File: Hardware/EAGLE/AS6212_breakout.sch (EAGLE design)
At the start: 19 parts, among them J2 QWIIC_RIGHT_ANGLE, J3 QWIIC_RIGHT_ANGLE, U1 AS6212

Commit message: v01 main push
Updated Eagle files and source software
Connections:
- net ADD1: now also J1.1; no longer J1.2
- net GND: now also J1.2; no longer J1.1
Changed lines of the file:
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@@
 <part name="P+2" library="supply1" library_urn="urn:adsk.eagle:library:371" deviceset="VCC" device=""/>
 <part name="P+3" library="supply1" library_urn="urn:adsk.eagle:library:371" deviceset="VCC" device=""/>
-<part name="GND3" library="supply1" library_urn="urn:adsk.eagle:library:371" deviceset="GND" device=""/>
 <part name="P+4" library="supply1" library_urn="urn:adsk.eagle:library:371" deviceset="VCC" device=""/>
 <part name="P+5" library="supply1" library_urn="urn:adsk.eagle:library:371" deviceset="VCC" device=""/>
@@
 <part name="R3" library="SparkFun-Resistors" deviceset="330OHM" device="-0603-1/10W-1%" value="330"/>
 <part name="JP7" library="SparkFun-Jumpers" deviceset="JUMPER-SMT_2_NC_TRACE" device="_SILK" package3d_urn="urn:adsk.eagle:package:39281/1"/>
+<part name="GND3" library="supply1" library_urn="urn:adsk.eagle:library:371" deviceset="GND" device=""/>
 </parts>
 <sheets>
@@
 <attribute name="VALUE" x="142.24" y="162.56" size="1.778" layer="96" rot="R180"/>
 </instance>
-<instance part="GND3" gate="1" x="139.7" y="139.7" smashed="yes">
-<attribute name="VALUE" x="137.16" y="137.16" size="1.778" layer="96"/>
-</instance>
 <instance part="P+4" gate="VCC" x="180.34" y="160.02" smashed="yes">
 <attribute name="VALUE" x="182.88" y="162.56" size="1.778" layer="96" rot="R180"/>
@@
 </instance>
 <instance part="JP7" gate="G$1" x="45.72" y="78.74" smashed="yes" rot="R90"/>
+<instance part="GND3" gate="1" x="147.32" y="139.7" smashed="yes">
+<attribute name="VALUE" x="144.78" y="137.16" size="1.778" layer="96"/>
+</instance>
 </instances>
 <busses>
@@
 </segment>
 <segment>
-<pinref part="J1" gate="G$1" pin="1"/>
-<wire x1="137.16" y1="144.78" x2="139.7" y2="144.78" width="0.1524" layer="91"/>
-<wire x1="139.7" y1="144.78" x2="139.7" y2="142.24" width="0.1524" layer="91"/>
-<pinref part="GND3" gate="1" pin="GND"/>
-</segment>
-<segment>
 <pinref part="J2" gate="G$1" pin="1"/>
 <wire x1="170.18" y1="144.78" x2="175.26" y2="144.78" width="0.1524" layer="91"/>
@@
 <wire x1="45.72" y1="63.5" x2="45.72" y2="60.96" width="0.1524" layer="91"/>
 </segment>
+<segment>
+<pinref part="J1" gate="G$1" pin="2"/>
+<pinref part="GND3" gate="1" pin="GND"/>
+<wire x1="137.16" y1="147.32" x2="147.32" y2="147.32" width="0.1524" layer="91"/>
+<wire x1="147.32" y1="147.32" x2="147.32" y2="142.24" width="0.1524" layer="91"/>
+</segment>
 </net>
 <net name="ADD1" class="0">
@@
 </segment>
 <segment>
-<pinref part="J1" gate="G$1" pin="2"/>
-<wire x1="137.16" y1="147.32" x2="139.7" y2="147.32" width="0.1524" layer="91"/>
-<label x="139.7" y="147.32" size="1.27" layer="95" xref="yes"/>
-</segment>
-<segment>
 <pinref part="JP6" gate="G$1" pin="2"/>
 <wire x1="195.58" y1="55.88" x2="198.12" y2="55.88" width="0.1524" layer="91"/>
 <label x="198.12" y="55.88" size="1.27" layer="95" xref="yes"/>
 </segment>
-</net>
+<segment>
+<pinref part="J1" gate="G$1" pin="1"/>
+<wire x1="137.16" y1="144.78" x2="139.7" y2="144.78" width="0.1524" layer="91"/>
+<label x="139.7" y="144.78" size="1.27" layer="95" xref="yes"/>
+</segment>
+</net>

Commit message: Rev 02 push
First production version of breakout board - push ready
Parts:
- R3: value 330 -> 10k; device SparkFun-Resistors:330OHM-0603-1/10W-1% -> SparkFun-Resistors:10KOHM-0603-1/10W-1%
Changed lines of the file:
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@@
 <part name="GND6" library="supply1" library_urn="urn:adsk.eagle:library:371" deviceset="GND" device=""/>
 <part name="P+7" library="supply1" library_urn="urn:adsk.eagle:library:371" deviceset="VCC" device=""/>
-<part name="R3" library="SparkFun-Resistors" deviceset="330OHM" device="-0603-1/10W-1%" value="330"/>
+<part name="R3" library="SparkFun-Resistors" deviceset="10KOHM" device="-0603-1/10W-1%" value="10k"/>
 <part name="JP7" library="SparkFun-Jumpers" deviceset="JUMPER-SMT_2_NC_TRACE" device="_SILK" package3d_urn="urn:adsk.eagle:package:39281/1"/>
 <part name="GND3" library="supply1" library_urn="urn:adsk.eagle:library:371" deviceset="GND" device=""/>

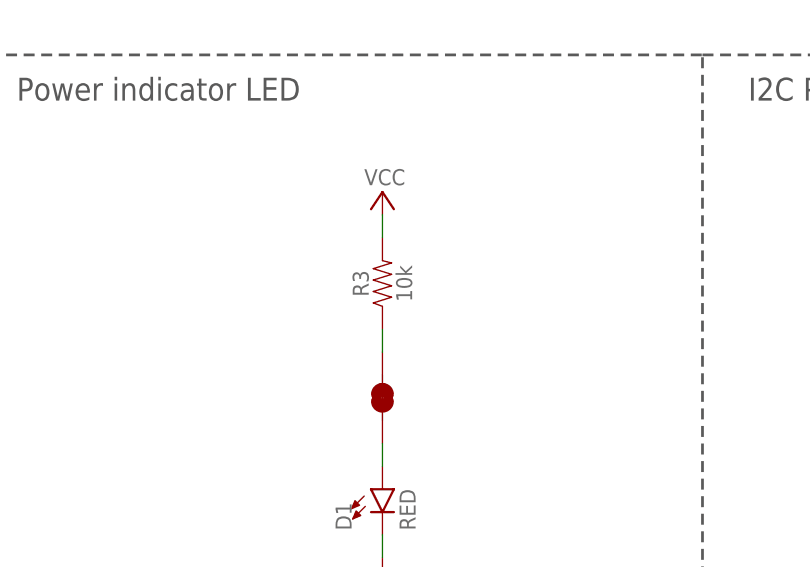
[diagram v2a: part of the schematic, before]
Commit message: Configuration register updates
small changes to software and hardware.
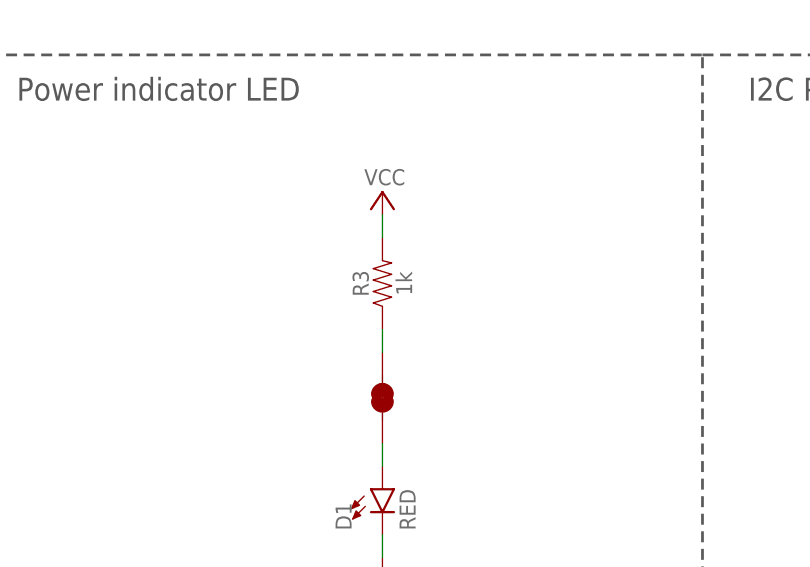
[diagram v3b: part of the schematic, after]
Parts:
- R3: value 10k -> 1k; device SparkFun-Resistors:10KOHM-0603-1/10W-1% -> SparkFun-Resistors:1KOHM-0603-1/10W-1%
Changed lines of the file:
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@@
 <part name="GND6" library="supply1" library_urn="urn:adsk.eagle:library:371" deviceset="GND" device=""/>
 <part name="P+7" library="supply1" library_urn="urn:adsk.eagle:library:371" deviceset="VCC" device=""/>
-<part name="R3" library="SparkFun-Resistors" deviceset="10KOHM" device="-0603-1/10W-1%" value="10k"/>
+<part name="R3" library="SparkFun-Resistors" deviceset="1KOHM" device="-0603-1/10W-1%" value="1k"/>
 <part name="JP7" library="SparkFun-Jumpers" deviceset="JUMPER-SMT_2_NC_TRACE" device="_SILK" package3d_urn="urn:adsk.eagle:package:39281/1"/>
 <part name="GND3" library="supply1" library_urn="urn:adsk.eagle:library:371" deviceset="GND" device=""/>

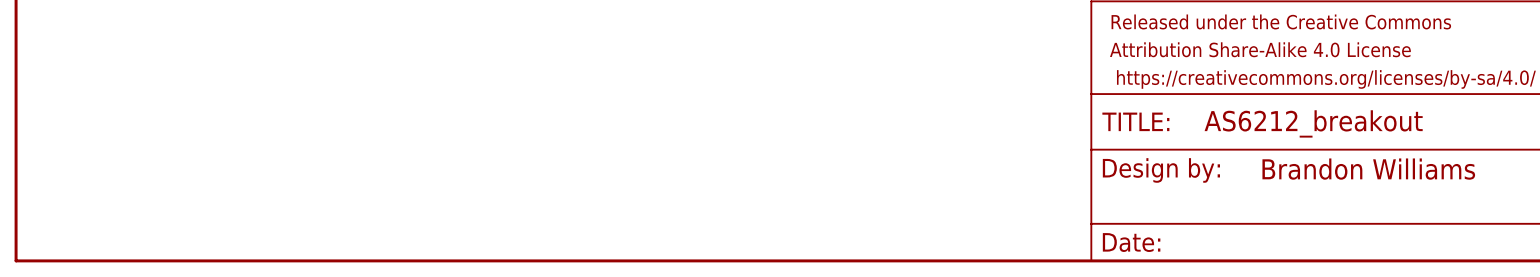
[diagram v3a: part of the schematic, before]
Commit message: Bug fixes
Added thank you in schematic as well
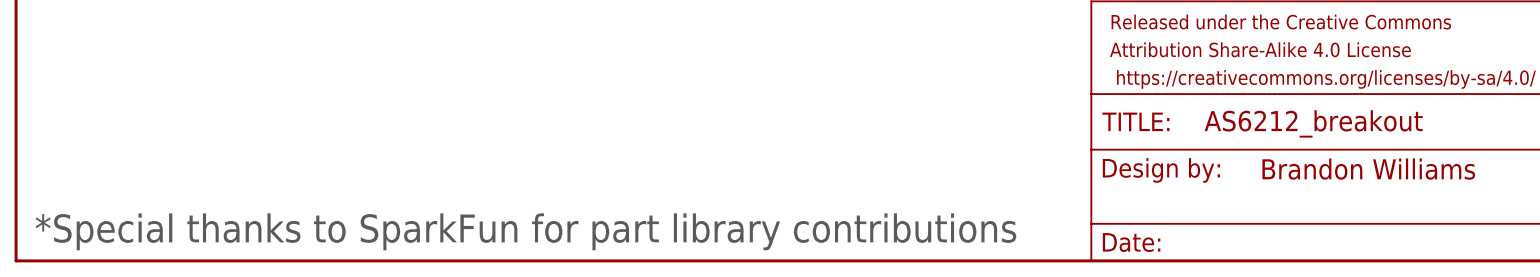
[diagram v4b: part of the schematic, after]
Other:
- note added: "*Special thanks to SparkFun for part library contributions"
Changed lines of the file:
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@@
 <text x="213.36" y="72.39" size="2.54" layer="97">0x4B</text>
 <text x="208.28" y="54.61" size="2.54" layer="97">Alert Enable</text>
+<text x="2.54" y="2.54" size="3.81" layer="97">*Special thanks to SparkFun for part library contributions</text>
 </plain>
 <instances>
